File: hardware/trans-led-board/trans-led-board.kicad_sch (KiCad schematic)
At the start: 7 parts, among them J1 Conn_01x02

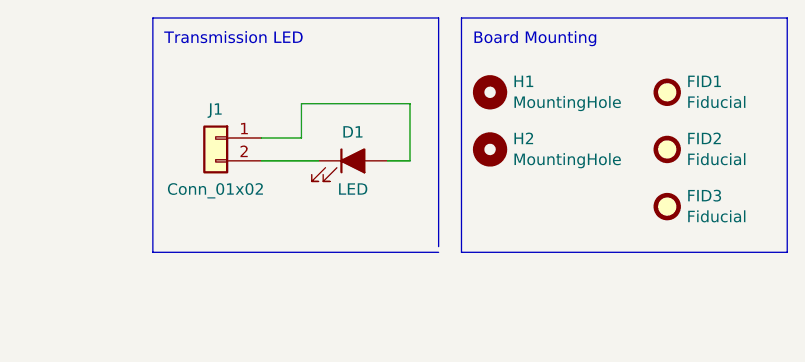
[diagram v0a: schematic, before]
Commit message: Merge hardware from spectrodensitometer project and rename
The spectrodensitometer R&D project is going to be used as the hardware
baseline, rather than the original DPD-100, because it has various
changes that will be useful to this project. Those changes include
different LEDs, different LED drivers, a temperature sensor, and a 1.8V
capable LDO.
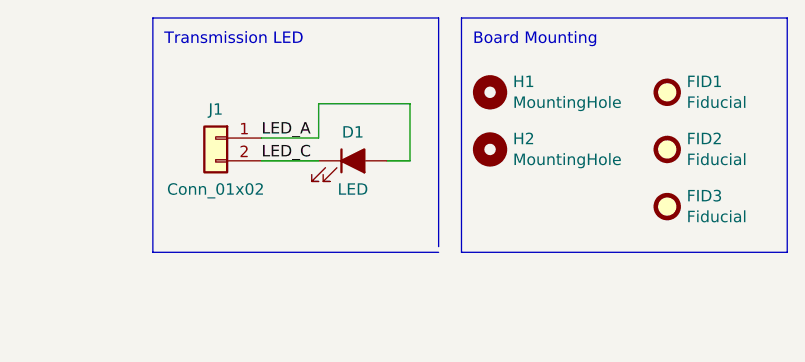
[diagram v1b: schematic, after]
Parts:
- D1: footprint lib_fp:LED_WL-SWTP-3022-1MP_ThermalVias -> lib_fp:SunLike_LED_S1S0; Manufacturer Würth Elektronik -> Seoul Semiconductor Inc.; Manufacturer PN 158302250 -> S1S0-3030659503-0000003S-0P001; Supplier Mouser -> Digi-Key; Supplier PN 710-158302250 -> 897-S1S0-3030659503-0000003S-0P001CT-ND
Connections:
- net LED_C: now reaches D1.1 (K), J1.2 (Pin_2)
- net LED_A: now reaches D1.2 (A), J1.1 (Pin_1)
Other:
- title: Printalyzer Densitometer - Transmission LED Board -> Printalyzer UV/VIS Densitometer - Transmission LED Board

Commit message: Designed updated transmission LED board with two UV LEDs
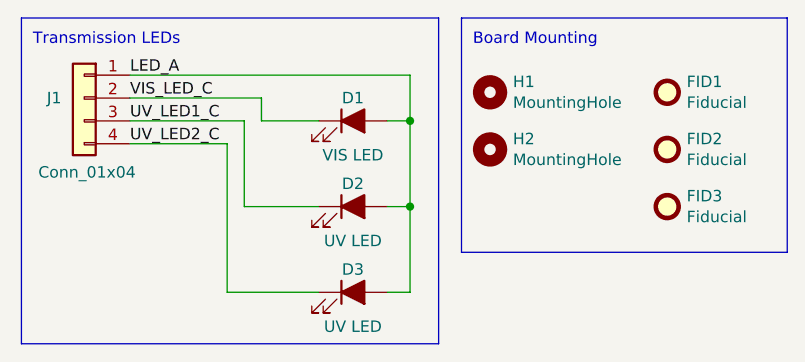
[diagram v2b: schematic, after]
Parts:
- removed J1: Conn_01x02, Connector_JST:JST_SH_SM02B-SRSS-TB_1x02-1MP_P1.00mm_Horizontal, symbol Connector_Generic:Conn_01x02
- added D2, D3: UV LED, LED_SMD:LED_PLCC_2835, symbol Device:LED_Filled
- added J1: Conn_01x04, Connector_JST:JST_SH_SM04B-SRSS-TB_1x04-1MP_P1.00mm_Horizontal, symbol Connector_Generic:Conn_01x04
- D1: value LED -> VIS LED; Manufacturer PN S1S0-3030659503-0000003S-0P001 -> S1S0-3030309503-0000003S-0P001; Supplier PN 897-S1S0-3030659503-0000003S-0P001CT-ND -> 897-S1S0-3030309503-0000003S-0P001CT-ND
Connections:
- net LED_A: now also D2.2 (A), D3.2 (A), J1.1 (Pin_1)
- net LED_C renamed VIS_LED_C
- net VIS_LED_C: now also J1.2 (Pin_2)
- new net UV_LED1_C: D2.1 (K), J1.3 (Pin_3)
- new net UV_LED2_C: D3.1 (K), J1.4 (Pin_4)
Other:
- note added: "Transmission LEDs"
- note removed: "Transmission LED"
- moved on the sheet: D1

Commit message: Clean up transmission board footprints
Added special narrow footprints for the transmission LEDs, and moved
them a little bit closer together.
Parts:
- D1: footprint lib_fp:SunLike_LED_S1S0 -> lib_fp:SunLike_LED_S1S0_Narrow
- D2, D3: footprint LED_SMD:LED_PLCC_2835 -> lib_fp:LED_WL-SUTW-2835_Narrow
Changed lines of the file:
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@@
       (effects (font (size 1.27 1.27)))
     )
-    (property "Footprint" "lib_fp:SunLike_LED_S1S0" (at 73.66 51.435 0)
+    (property "Footprint" "lib_fp:SunLike_LED_S1S0_Narrow" (at 73.66 51.435 0)
       (effects (font (size 1.27 1.27)) hide)
     )
@@
       (effects (font (size 1.27 1.27)))
     )
-    (property "Footprint" "LED_SMD:LED_PLCC_2835" (at 73.66 70.485 0)
+    (property "Footprint" "lib_fp:LED_WL-SUTW-2835_Narrow" (at 73.66 70.485 0)
       (effects (font (size 1.27 1.27)) hide)
     )
@@
       (effects (font (size 1.27 1.27)))
     )
-    (property "Footprint" "LED_SMD:LED_PLCC_2835" (at 73.66 60.96 0)
-      (effects (font (size 1.27 1.27)) hide)
-    )
+    (property "Footprint" "lib_fp:LED_WL-SUTW-2835_Narrow" (at 73.66 60.96 0)
+      (effects (font (size 1.27 1.27)) hide)
+    )
